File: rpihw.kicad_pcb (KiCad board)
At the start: 4 copper layers, 207 x 78.7 mm, 101 parts, among them P1 CONN_01X02, P101 CONN_01X02, P102 CONN_01X02, P103 CONN_01X08, P2 CONN_01X02, P3 CONN_02X20, Q1 2N3904BU, Q2 2N3904BU, Q3 2N3904BU, Q4 2N3904BU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

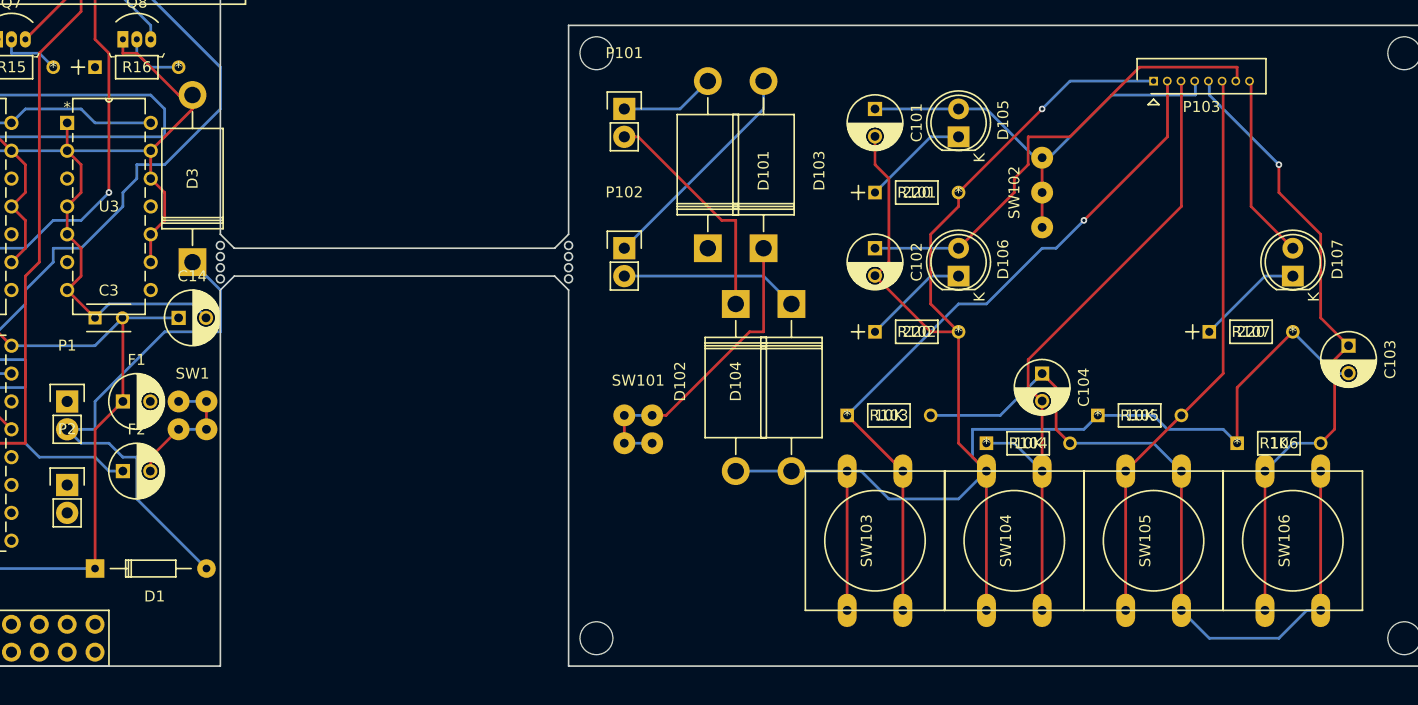
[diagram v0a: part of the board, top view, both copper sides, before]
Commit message: Improve switch footprints, add beveled 3D model.
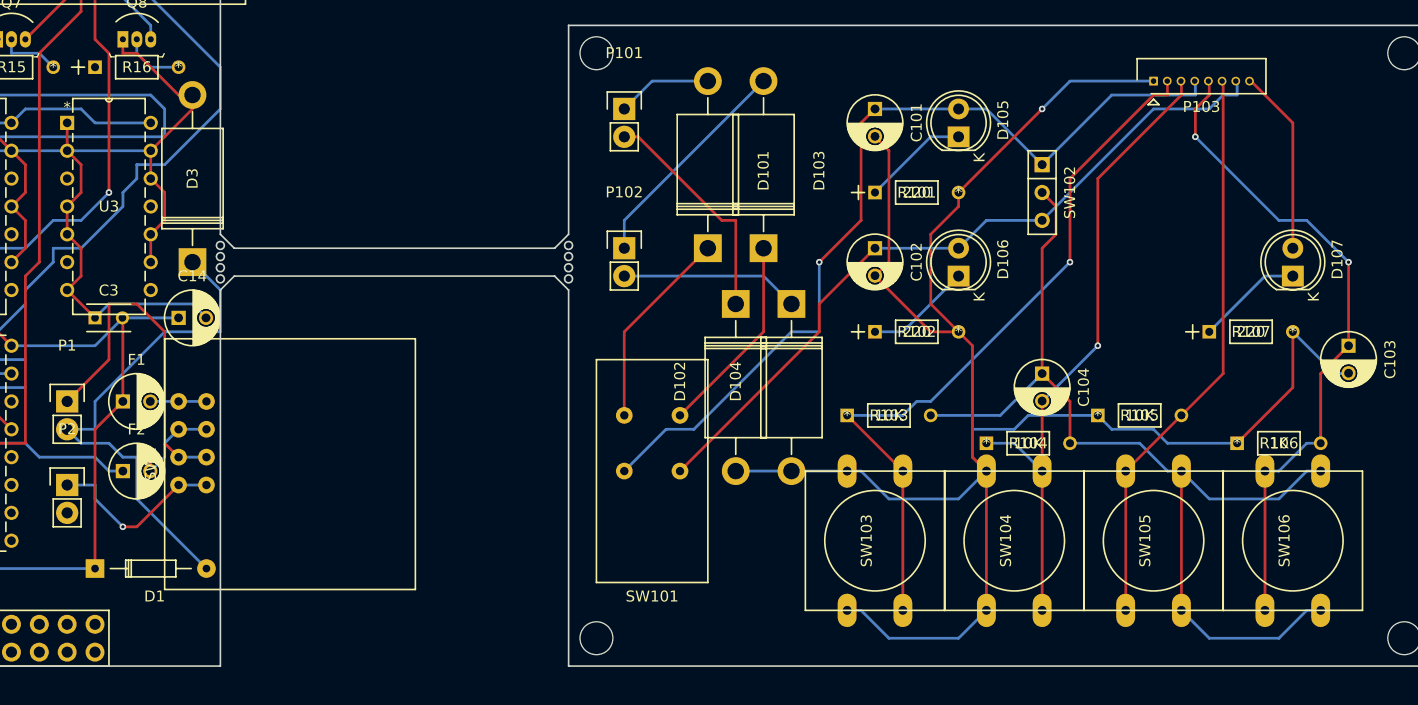
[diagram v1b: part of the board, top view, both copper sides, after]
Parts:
- SW1: footprint Wire_Pads:SolderWirePad_4xSquare_0-8mmDrill -> rpihw:Hack_S201
- SW101: footprint Wire_Pads:SolderWirePad_4xSquare_0-8mmDrill -> rpihw:Hack_L201
- SW102: footprint Wire_Pads:SolderWirePad_3x_0-8mmDrill -> Buttons_Switches_ThroughHole:SW_Micro_SPST
- moved SW1 4.62 mm to (146.1, 98.4)
- moved SW101 4.02 mm to (189.2, 99.1), turned to 180 degrees
- turned SW102 to 270 degrees
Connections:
- SW1 pad 1: Net-(F2-Pad2) -> Net-(P2-Pad1)
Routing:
- net Net-(C101-Pad1): track 42.9 -> 80.7 mm, vias 0 -> 1
- net Net-(P1-Pad1): track 0.00 -> 31.1 mm
- net Net-(C102-Pad1): track 43.5 -> 67.9 mm
- net Net-(C104-Pad1): track 70.6 -> 90.2 mm
- net Net-(D101-Pad1): track 0.00 -> 18.4 mm
- net Net-(P2-Pad1): track 0.00 -> 16.6 mm, vias 0 -> 1
- net Net-(D103-Pad1): track 28.6 -> 18.4 mm
- net Net-(F1-Pad2): track 0.00 -> 5.12 mm
- net Net-(F2-Pad2): track 12.5 -> 8.75 mm
- net Net-(C103-Pad1): track 58.2 -> 60.8 mm, vias 1 -> 2
- net Net-(P103-Pad2): track 64.7 -> 66.9 mm
- net Net-(C101-Pad2): track 173.5 -> 175.6 mm
- net Net-(C104-Pad2): track 60.8 -> 59.8 mm, vias 0 -> 1
